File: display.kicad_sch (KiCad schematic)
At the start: 27 parts, among them J10 HDMI-A_WE_685119134923, J9 JST_SM_1x10_SM10B-SURS-TF-LF-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

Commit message: [#54617] Move LVDS display related components to separate repo
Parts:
- removed C61: C_100n_0402, antmicro-footprints:C_0402_1005Metric, symbol antmicroCapacitors0402:C_100n_0402
- removed C?: C_4u7_0402, antmicro-footprints:C_0402_1005Metric, symbol antmicroCapacitors0402:C_4u7_0402
- removed D? (x2): PUSB3F96X_PASS, antmicro-footprints:Nexperia_DFN-10_2.5x1mm_P0.5mm, symbol antmicroTVSDiodes:PUSB3F96X_PASS
- removed J9: JST_SM_1x10_SM10B-SURS-TF-LF-SN, antmicro-footprints:Conn_JST_SUR_1x10_SM10B-SURS-TF-LF-SN, symbol antmicroWire2BoardConnectors:JST_SUR_1x10_SM10B-SURS-TF-LF-SN
- removed J?: F52R-1A7H1-11020, antmicro-footprints:F52R-1A7H1-11020, symbol antmicroFCCConnectors:F52R-1A7H1-11020
- removed TP? (x3): TP_0.75mm_SMD, antmicro-footprints:TP_SMD_0.75mm, symbol antmicroTestPoints:TP_0.75mm_SMD
- added C1, C3: C_10u_0402, antmicro-footprints:C_0402_1005Metric, symbol antmicroCapacitors0402:C_10u_0402
- added D1, D3, D4: PUSB3F96X_PASS, antmicro-footprints:Nexperia_DFN-10_2.5x1mm_P0.5mm, symbol antmicroTVSDiodes:PUSB3F96X_PASS
- added D6: TPD1E0B04_XDFN-2, antmicro-footprints:XDFN-2_1x0.60mm, symbol antmicroTVSDiodes:TPD1E0B04_XDFN-2
- added FB4: FB_220Z_2.2A_TDK-MPZ_0603, antmicro-footprints:FB_0603_1608Metric, symbol antmicroFerriteBeadsandChips:FB_220Z_2.2A_TDK-MPZ_0603
- added J12: Socket_Molex_SlimStack_2x15_541020304, antmicro-footprints:Conn_Socket_Molex_SlimStack_2x15_541020304, symbol antmicroB2BConnectors:Socket_Molex_SlimStack_2x15_541020304
- added L1, L2, L3, L4, L5: NFP0QHB242HS2D, antmicro-footprints:Choke_025020_0605Metric, symbol antmicroCommonModeChokes:Choke_NFP0QHB242HS2D
- added R1, R2: R_4x100R_0402_array, antmicro-footprints:R_Array_4x0402_Panasonic_EXB28V, symbol antmicroResistorNetworksArrays:R_4x100R_0402_array
- D? (x3): DNP DNP -> (none)
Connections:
- net DisplayCtrl.SCL is gone; now on net GND: D?.5 (CH4), D?.6 (CH4)
- net DisplayCtrl.SDA is gone; now on net GND: D?.4 (CH3), D?.7 (CH3)
- net +3V3: now also C3.2, D6.2, J12.12
- net +5V: now also FB4.1
- net DSI.CLK_N: now also L5.4
- net DSI.CLK_P: now also L5.1
- net DSI.D0_N: now also L4.4
- net DSI.D0_P: now also L4.1
- net DSI.D1_N: now also L3.4
- net DSI.D1_P: now also L3.1
- net DSI.D2_N: now also L2.4
- net DSI.D2_P: now also L2.1
- net DSI.D3_N: now also L1.4
- net DSI.D3_P: now also L1.1
- net GND: now also C1.1, C3.1, D1.3 (GND), D1.8 (GND), D3.3 (GND), D3.8 (GND), D4.3 (GND), D4.8 (GND), D6.1, J12.11, J12.14, J12.17, J12.2, J12.23, J12.29, J12.5
- new net: J12.1, L1.3
- new net: C1.2, D4.1 (CH1), D4.10 (CH1), D4.2 (CH2), D4.4 (CH3), D4.5 (CH4), D4.6 (CH4), D4.7 (CH3), D4.9 (CH2), FB4.2, J12.10, J12.4, J12.6, J12.8
- new net: J12.13, L3.3
- new net: J12.15, L3.2
- new net: J12.16, R1.1 (R1.1)
- new net: J12.18, R1.2 (R2.1)
- new net: J12.19, L4.3
- new net: J12.20, R1.3 (R3.1)
- new net: J12.21, L4.2
- new net: J12.22, R1.4 (R4.1)
- new net: J12.24, R2.1 (R1.1)
- new net: J12.25, L5.3
- new net: J12.26, R2.2 (R2.1)
- new net: J12.27, L5.2
- new net: J12.28, R2.3 (R3.1)
- new net: J12.3, L1.2
- new net: J12.30, R2.4 (R4.1)
- new net: J12.7, L2.3
- new net: J12.9, L2.2
- new net AntmUD.DIM: D3.4 (CH3), D3.7 (CH3), R2.6 (R3.2)
- new net AntmUD.EN: D3.1 (CH1), D3.10 (CH1), R2.8 (R1.2)
- new net AntmUD.GPIO: D3.5 (CH4), D3.6 (CH4), R2.5 (R4.2)
- new net AntmUD.IRQ1: D1.4 (CH3), D1.7 (CH3), R1.6 (R3.2)
- new net AntmUD.SCL: D1.2 (CH2), D1.9 (CH2), R1.7 (R2.2)
- new net AntmUD.SDA: D1.1 (CH1), D1.10 (CH1), R1.8 (R1.2)
- new net AntmUD.~{IRQ2}: D1.5 (CH4), D1.6 (CH4), R1.5 (R4.2)
- new net AntmUD.~{RST}: D3.2 (CH2), D3.9 (CH2), R2.7 (R2.2)
- no-connect marks 3 -> 1
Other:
- removed sheet DSI -> LVDS converter
- removed sheet LVDS display
- note added: "AntmUD Connector"
- note removed: "DSI -> LVDS"
- note removed: "DSI Connector"
- note removed: "I2C touchscreen connector"
- note removed: "LVDS connector"
- note removed: "Note: IO's are 3V3 level"
- note removed: "assembly option for DSI connector, if LVDS is not used (pass-through to LVDS converter)"
- moved on the sheet: C?, D21, D?, FB3, J10, L?, R?

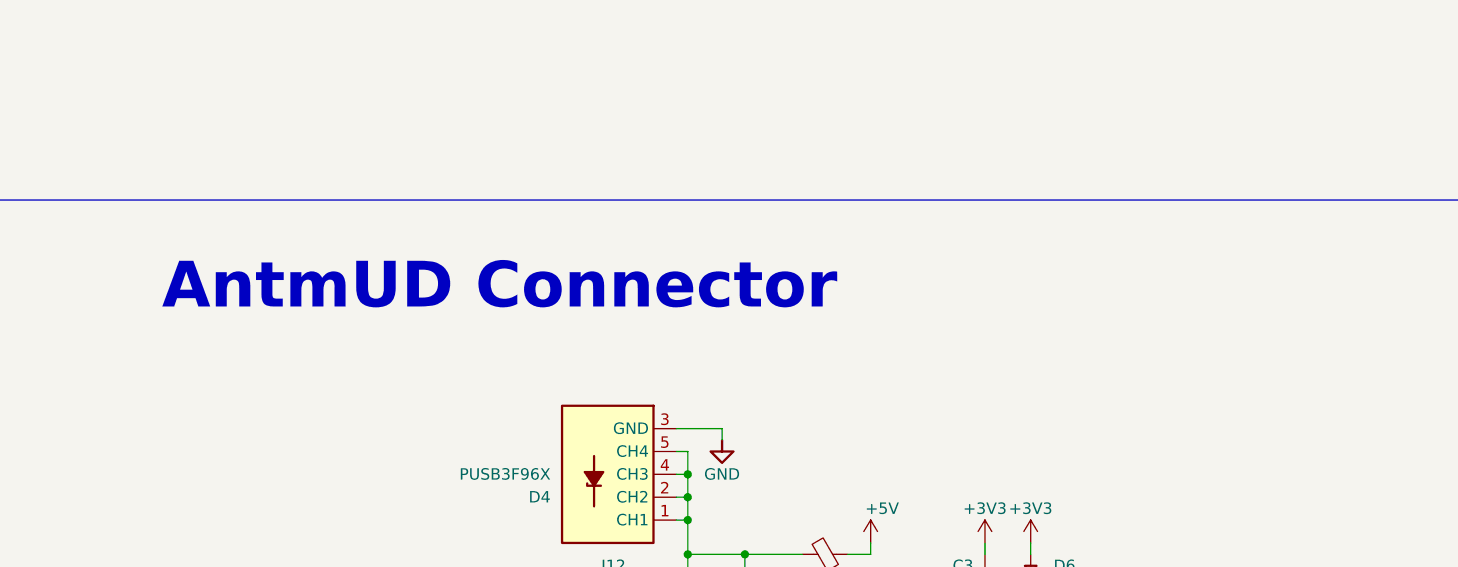
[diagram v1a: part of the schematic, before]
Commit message: [#54617] Update bus naming; remove DNP for TVS
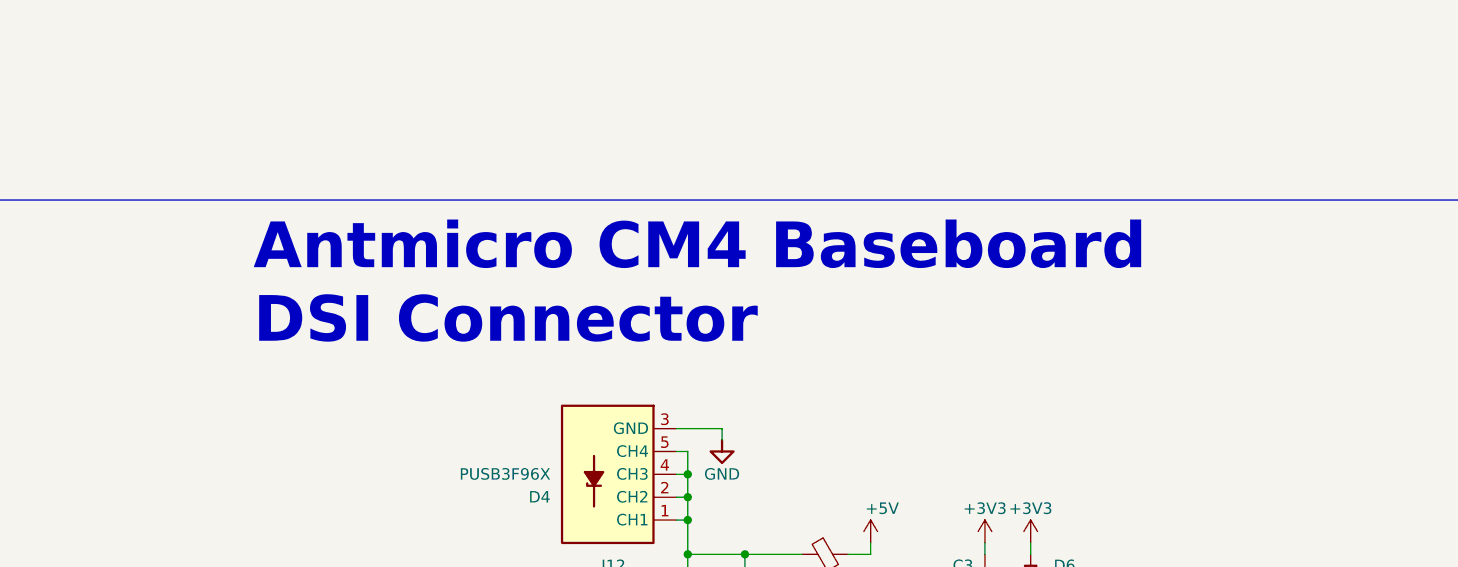
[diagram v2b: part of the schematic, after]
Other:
- note added: "Antmicro CM4 Baseboard DSI Connector"
- note removed: "AntmUD Connector"
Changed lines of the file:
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@@
     (effects (font (size 5.08 5.08) (thickness 1.016) bold) (justify left bottom))
   )
-  (text "AntmUD Connector" (at 177.8 147.32 0)
+  (text "Antmicro CM4 Baseboard\nDSI Connector" (at 187.96 151.13 0)
     (effects (font (size 5.08 5.08) (thickness 1.016) bold) (justify left bottom))
   )
@@
     (effects (font (size 1.27 1.27)) (justify left bottom))
   )
-  (label "AntmUD.EN" (at 252.73 210.82 0)
+  (label "AntmUD.EN" (at 252.73 210.82 0) (fields_autoplaced)
     (effects (font (size 1.27 1.27)) (justify left bottom))
   )
@@
     (effects (font (size 1.27 1.27)) (justify left bottom))
   )
-  (label "AntmUD.GPIO" (at 252.73 218.44 0)
+  (label "AntmUD.GPIO" (at 252.73 218.44 0) (fields_autoplaced)
     (effects (font (size 1.27 1.27)) (justify left bottom))
   )
@@
     (effects (font (size 1.27 1.27)) (justify left bottom))
   )
-  (label "AntmUD.~{IRQ2}" (at 252.73 208.28 0)
+  (label "AntmUD.~{IRQ2}" (at 252.73 208.28 0) (fields_autoplaced)
     (effects (font (size 1.27 1.27)) (justify left bottom))
   )
@@
     (effects (font (size 1.27 1.27)) (justify left bottom))
   )
-  (label "AntmUD.IRQ1" (at 252.73 205.74 0)
+  (label "AntmUD.IRQ1" (at 252.73 205.74 0) (fields_autoplaced)
     (effects (font (size 1.27 1.27)) (justify left bottom))
   )
@@
     (effects (font (size 1.27 1.27)) (justify left bottom))
   )
-  (label "AntmUD.~{RST}" (at 252.73 213.36 0)
+  (label "AntmUD.~{RST}" (at 252.73 213.36 0) (fields_autoplaced)
     (effects (font (size 1.27 1.27)) (justify left bottom))
   )
@@
     (effects (font (size 1.27 1.27)) (justify left bottom))
   )
-  (label "AntmUD.DIM" (at 252.73 215.9 0)
+  (label "AntmUD.DIM" (at 252.73 215.9 0) (fields_autoplaced)
     (effects (font (size 1.27 1.27)) (justify left bottom))
   )

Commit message: [#54617] Review requested changes
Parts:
- D6: MPN TPD1E0B04DPYR -> TPD1E0B04DPYR
- R1, R2: Val 4x100R -> R_4x100R_0402
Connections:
- net AntmUD.DIM renamed DSICtrl.DIM
- net AntmUD.EN renamed DSICtrl.EN
- net AntmUD.GPIO renamed DSICtrl.GPIO
- net AntmUD.IRQ1 renamed DSICtrl.IRQ1
- net AntmUD.SCL renamed DSICtrl.SCL
- net AntmUD.SDA renamed DSICtrl.SDA
- net AntmUD.~{IRQ2} renamed DSICtrl.~{IRQ2}
- net AntmUD.~{RST} renamed DSICtrl.~{RST}
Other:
- note added: "DSICtrl Connector"
- note removed: "Antmicro CM4 Baseboard DSI Connector"

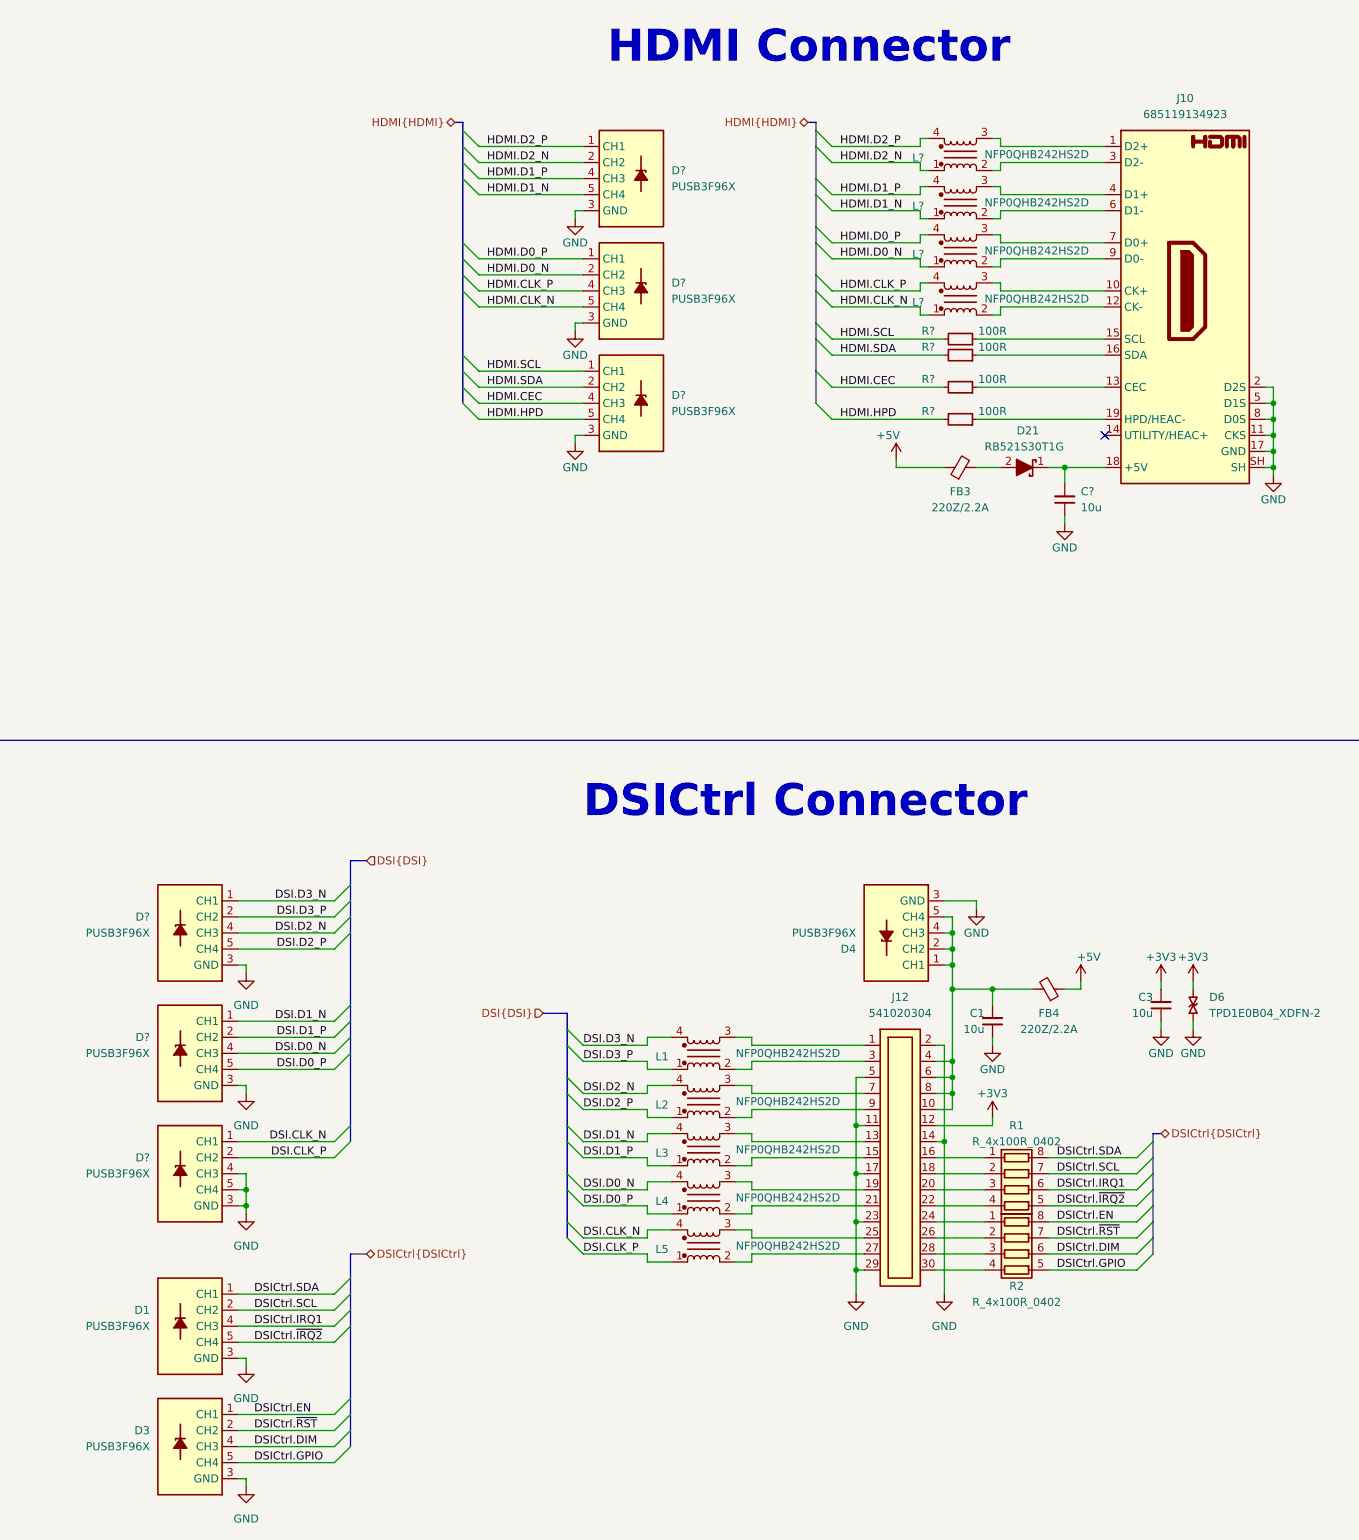
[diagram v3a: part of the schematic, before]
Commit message: [#54617] Re-enumerate reference designators
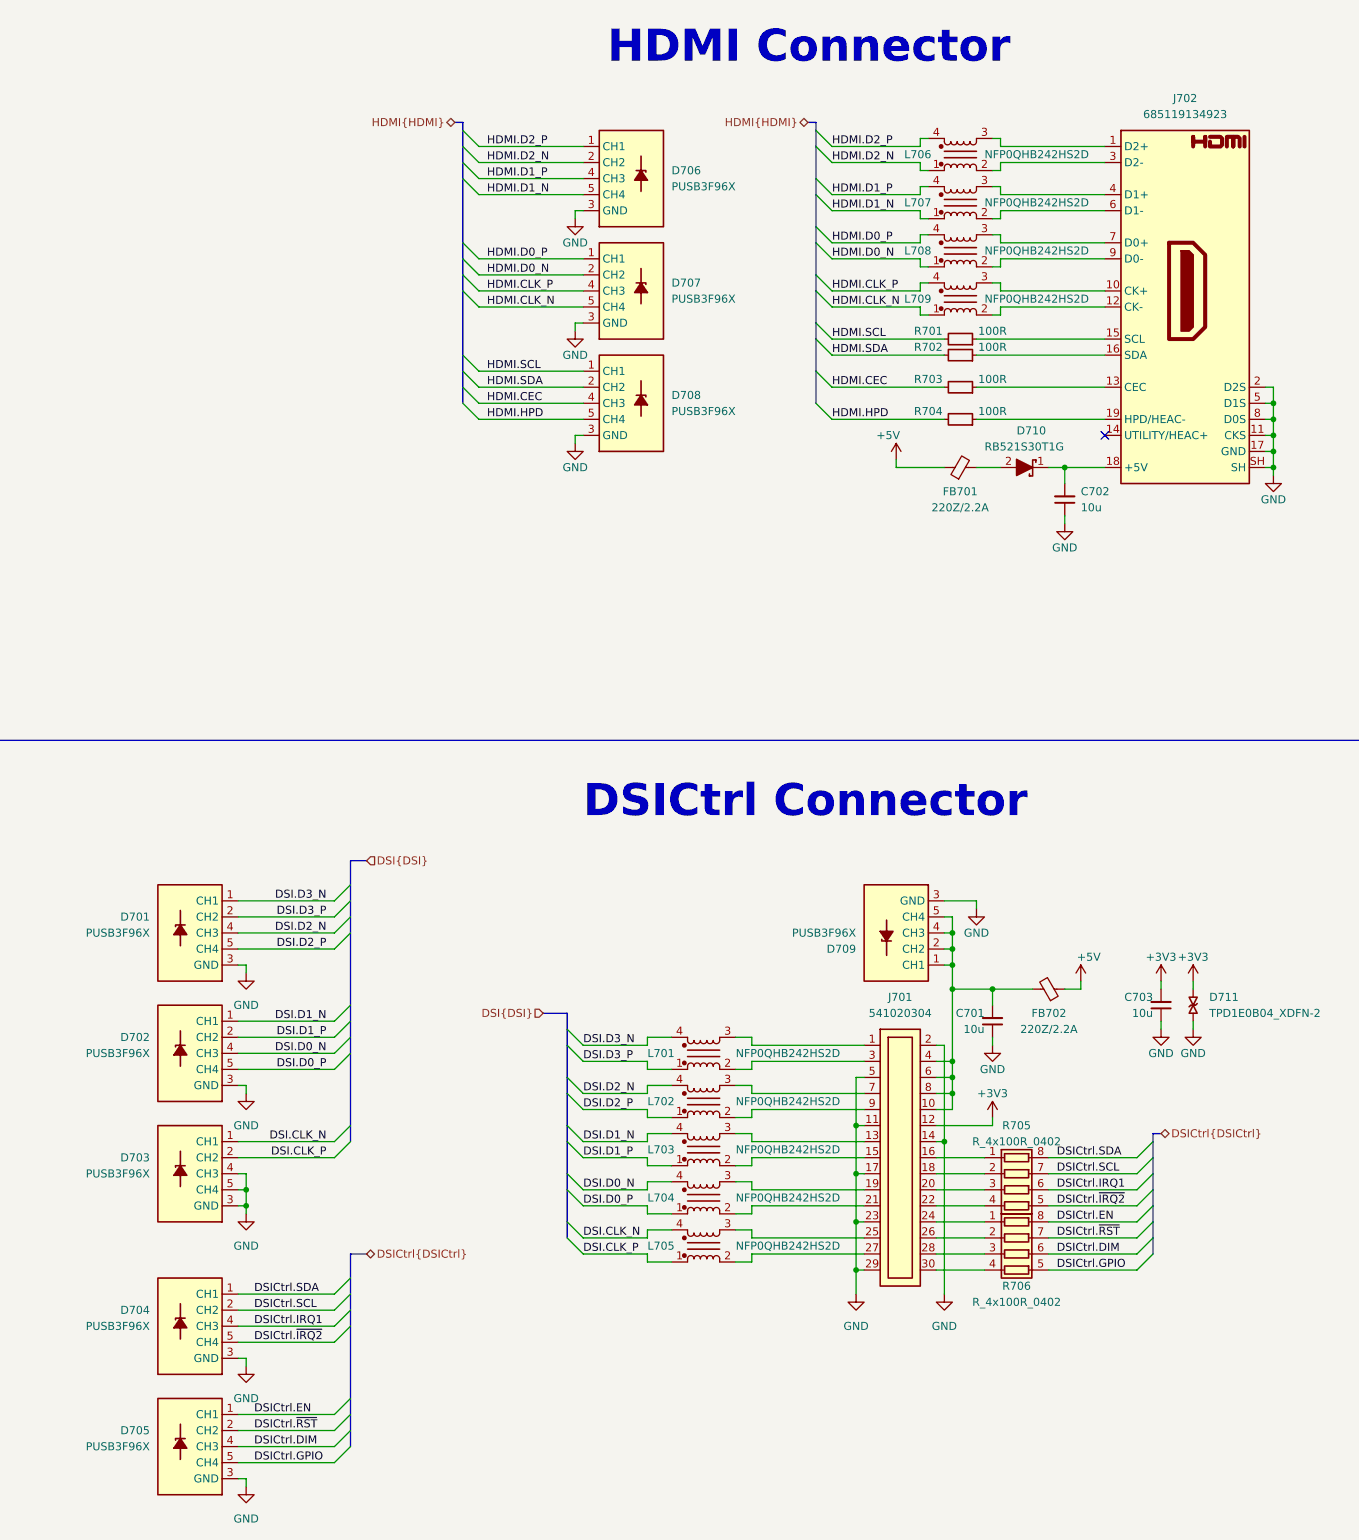
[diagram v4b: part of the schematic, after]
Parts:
- gave numbers to parts that had none: 15
- renumbered C1 to C701, C3 to C703, D1 to D704, D3 to D705, D4 to D709, D21 to D710, D6 to D711, FB3 to FB701, FB4 to FB702, J12 to J701, J10 to J702, L1 to L701, L2 to L702, L3 to L703, L4 to L704, L5 to L705, R1 to R705, R2 to R706
